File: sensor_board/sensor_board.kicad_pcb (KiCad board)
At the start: 2 copper layers, 10.2 x 10.2 mm, 4 parts, among them U1 TSL25911FN

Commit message: layout edits
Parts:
- BlackbodyC1: footprint blackbodies:CONN_SD-105310-100_04_MOL -> blackbodies:CONN_SD-105429-001_04_MOL
- moved C4 2.93 mm to (107.2, 53.7)
- moved R1 2.92 mm to (112.7, 53.7), turned to -90 degrees
- moved U1 2.80 mm to (110.0, 53.7)
- moved BlackbodyC1 1.27 mm to (110.0, 53.7)
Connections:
- BlackbodyC1 pad 1: /SDA -> /SCL
- BlackbodyC1 pad 2: /SCL -> /SDA
- BlackbodyC1 pad 3: +3V3 -> GND
- BlackbodyC1 pad 4: GND -> +3V3
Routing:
- net +3V3: track 15.0 -> 10.3 mm, vias 0 -> 1
- net GND: track 15.1 -> 11.1 mm, vias 0 -> 2
- net /SDA: track 2.59 -> 2.81 mm, vias 0 -> 1
- net /SCL: track 2.57 -> 2.74 mm, vias 0 -> 1
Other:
- board size 10.2 x 10.2 mm -> 10.2 x 10.3 mm

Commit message: layout updates
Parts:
- added Power1: D, LED_SMD:LED_0805_2012Metric, F.Cu at (112.9, 50.7)
- added R2: 2k, Resistor_SMD:R_0805_2012Metric, F.Cu at (107.3, 50.7)
- C4: footprint Capacitor_SMD:C_0402_1005Metric -> Capacitor_SMD:C_0805_2012Metric
- R1: footprint Resistor_SMD:R_0402_1005Metric -> Resistor_SMD:R_0805_2012Metric
- moved C4 0.94 mm to (106.8, 54.5)
- moved R1 0.85 mm to (112.8, 54.5)
- moved U1 0.85 mm to (110.0, 54.5)
- moved BlackbodyC1 0.10 mm to (110.0, 53.5)
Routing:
- net Net-(Power1-A): track 0.00 -> 5.61 mm
- net +3V3: track 10.3 -> 13.2 mm
- net /SDA: track 2.81 -> 1.91 mm
- net /SCL: track 2.74 -> 1.86 mm
- net GND: vias 2 -> 3
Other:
- board size 10.2 x 10.3 mm -> 9.3 x 12.3 mm

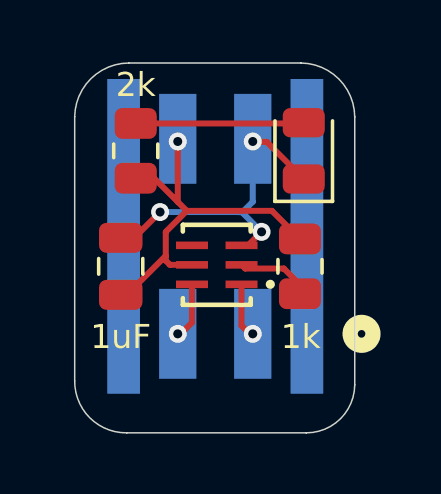
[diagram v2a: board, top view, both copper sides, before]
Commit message: fixed footprint issue
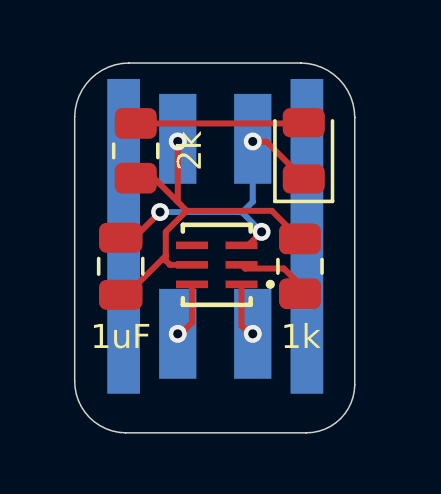
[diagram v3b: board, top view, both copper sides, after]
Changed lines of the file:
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@@
 		)
 		(property "Value" "2k"
-			(at 2.2 0 180)
+			(at 0 1.8 270)
 			(layer "F.SilkS")
 			(effects
@@
 		(sheetfile "sensor_board.kicad_sch")
 		(attr smd)
-		(fp_circle
-			(center 4.8768 3.250001)
-			(end 5.2578 3.250001)
-			(stroke
-				(width 0.508)
-				(type solid)
-			)
-			(fill no)
-			(layer "F.SilkS")
-		)
 		(fp_line
 			(start -4.2418 -3.1115)
@@
 			)
 			(layer "B.SilkS")
-		)
-		(fp_circle
-			(center 4.8768 3.250001)
-			(end 5.2578 3.250001)
-			(stroke
-				(width 0.508)
-				(type solid)
-			)
-			(fill no)
-			(layer "B.SilkS")
-		)
-		(fp_line
-			(start -4.3688 -5.4991)
-			(end 4.3688 -5.4991)
-			(stroke
-				(width 0.1524)
-				(type solid)
-			)
-			(layer "B.CrtYd")
-		)
-		(fp_line
-			(start -4.3688 6.4389)
-			(end -4.3688 -5.4991)
-			(stroke
-				(width 0.1524)
-				(type solid)
-			)
-			(layer "B.CrtYd")
-		)
-		(fp_line
-			(start 4.3688 -5.4991)
-			(end 4.3688 6.4389)
-			(stroke
-				(width 0.1524)
-				(type solid)
-			)
-			(layer "B.CrtYd")
-		)
-		(fp_line
-			(start 4.3688 6.4389)
-			(end -4.3688 6.4389)
-			(stroke
-				(width 0.1524)
-				(type solid)
-			)
-			(layer "B.CrtYd")
 		)
 		(fp_line
@@
 	)
 	(gr_arc
-		(start 112.810421 47.772408)
-		(mid 114.072408 48.307379)
-		(end 114.6 49.572468)
+		(start 112.810421 47.772417)
+		(mid 114.082076 48.31718)
+		(end 114.6 49.6)
 		(stroke
 			(width 0.05)
@@
 	)
 	(gr_arc
-		(start 107.00074 60.100054)
-		(mid 105.76965 59.600024)
-		(end 105.264834 58.370889)
+		(start 106.960025 60.1)
+		(mid 105.755259 59.585493)
+		(end 105.264834 58.370725)
 		(stroke
 			(width 0.05)
@@
 	)
 	(gr_arc
-		(start 105.265029 49.561987)
-		(mid 105.8 48.3)
-		(end 107.065089 47.772408)
+		(start 105.26503 49.561987)
+		(mid 105.800432 48.299563)
+		(end 107.066322 47.772408)
 		(stroke
 			(width 0.05)
@@
 	(gr_line
 		(start 112.986525 60.1)
-		(end 107.000739 60.1)
+		(end 106.960109 60.1)
 		(stroke
 			(width 0.05)
@@
 	(gr_arc
 		(start 114.6 58.5)
-		(mid 114.122215 59.632266)
-		(end 112.985786 60.100063)
+		(mid 114.122219 59.63227)
+		(end 112.985786 60.100062)
 		(stroke
 			(width 0.05)
